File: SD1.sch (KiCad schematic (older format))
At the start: 44 parts, among them J103 JST ZH 1.5mm 1x5, J107 FPC PMS, Q101 BSS138, Q102 PDTC114EU,115, SW103 Multidirection_Switch, U102 ER-TFTM028-4, U104 CC2652P, U106 EKMC1691111, U107 MCP23017, U108 BME280, U109 SCD30

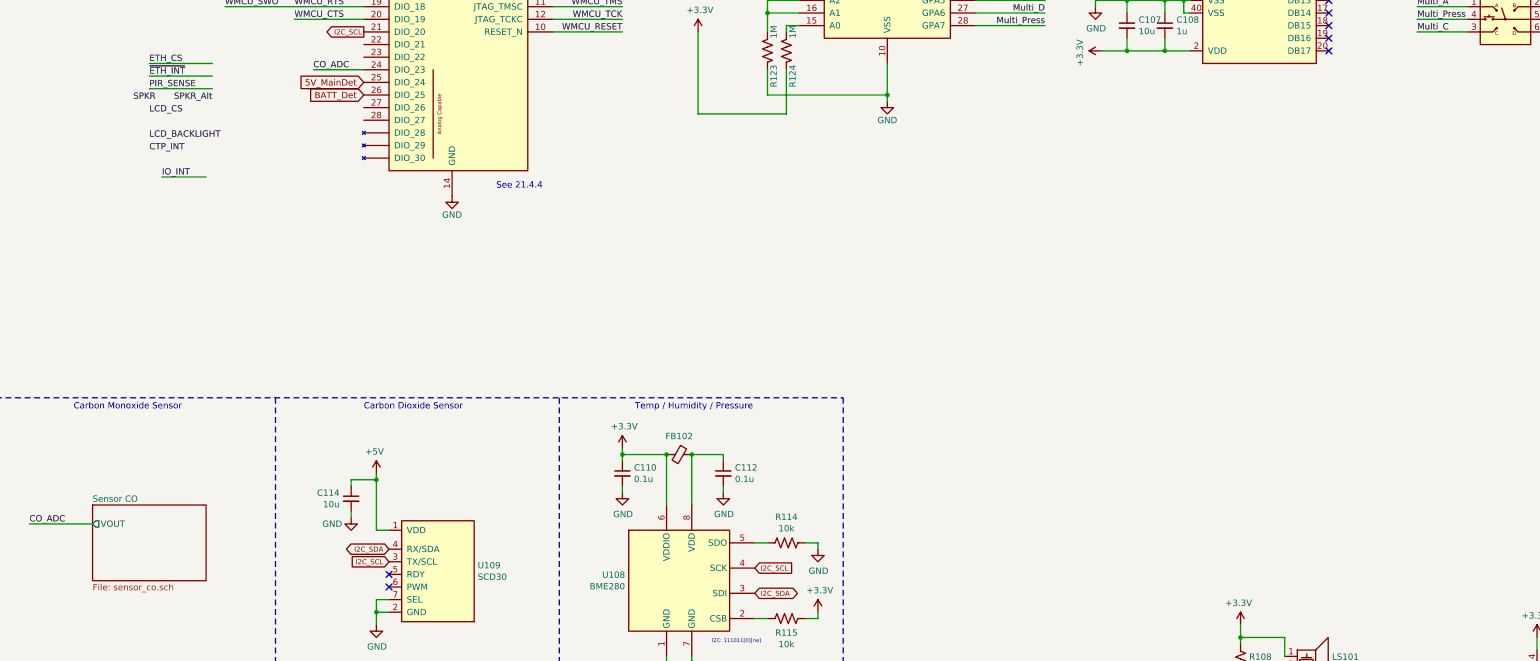
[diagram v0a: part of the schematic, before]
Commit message: Cleaned up, Annotated
Added Global 5V_Main net, solder jumper for battery charger, jumper for speaker and speaker_alt, added parts for battery charger
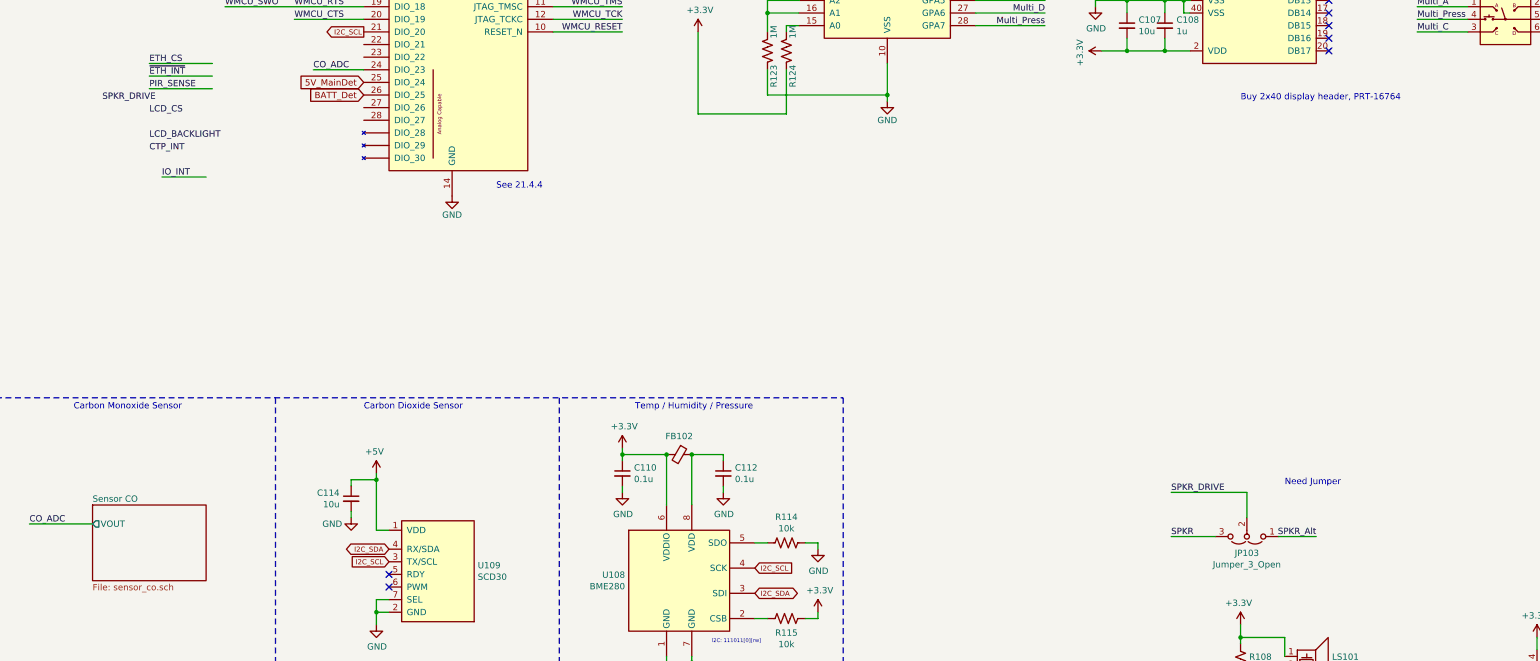
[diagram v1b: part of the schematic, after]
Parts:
- added JP103: Jumper_3_Open, Connector_PinHeader_2.54mm:PinHeader_1x03_P2.54mm_Vertical, symbol Jumper:Jumper_3_Open
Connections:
- net SPKR: now also JP103.3 (B)
- net SPKR_Alt: now also JP103.1 (A)
- new net SPKR_DRIVE: JP103.2 (C)
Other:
- note added: "Buy 2x40 display header, PRT-16764"
- note added: "Need Jumper"
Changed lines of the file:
@@
 Text Label 11200 3350 2    50   ~ 0
 Multi_Press
-Text Label 4600 3950 2    50   ~ 0
-SPKR_Alt
 Text Label 4150 3950 2    50   ~ 0
-SPKR
+SPKR_DRIVE
 Wire Wire Line
 	11150 2150 10650 2150
@@
 Wire Wire Line
 	15400 2500 15400 2550
+Text Notes 12750 3950 0    50   ~ 0
+Buy 2x40 display header, PRT-16764
+$Comp
+L Jumper:Jumper_3_Open JP103
+U 1 1 5FE23178
+P 12800 7400
+F 0 "JP103" H 12800 7531 50  0000 C CNN
+F 1 "Jumper_3_Open" H 12800 7622 50  0000 C CNN
+F 2 "Connector_PinHeader_2.54mm:PinHeader_1x03_P2.54mm_Vertical" H 12800 7400 50  0001 C CNN
+F 3 "~" H 12800 7400 50  0001 C CNN
+	1    12800 7400
+	-1   0    0    1
+$EndComp
+Wire Wire Line
+	12800 7250 12800 7050
+Wire Wire Line
+	12800 7050 12200 7050
+Wire Wire Line
+	13050 7400 13350 7400
+Wire Wire Line
+	12550 7400 12200 7400
+Text Label 12200 7400 0    50   ~ 0
+SPKR
+Text Label 13350 7400 2    50   ~ 0
+SPKR_Alt
+Text Label 12200 7050 0    50   ~ 0
+SPKR_DRIVE
+Text Notes 13100 7000 0    50   ~ 0
+Need Jumper
 $EndSCHEMATC

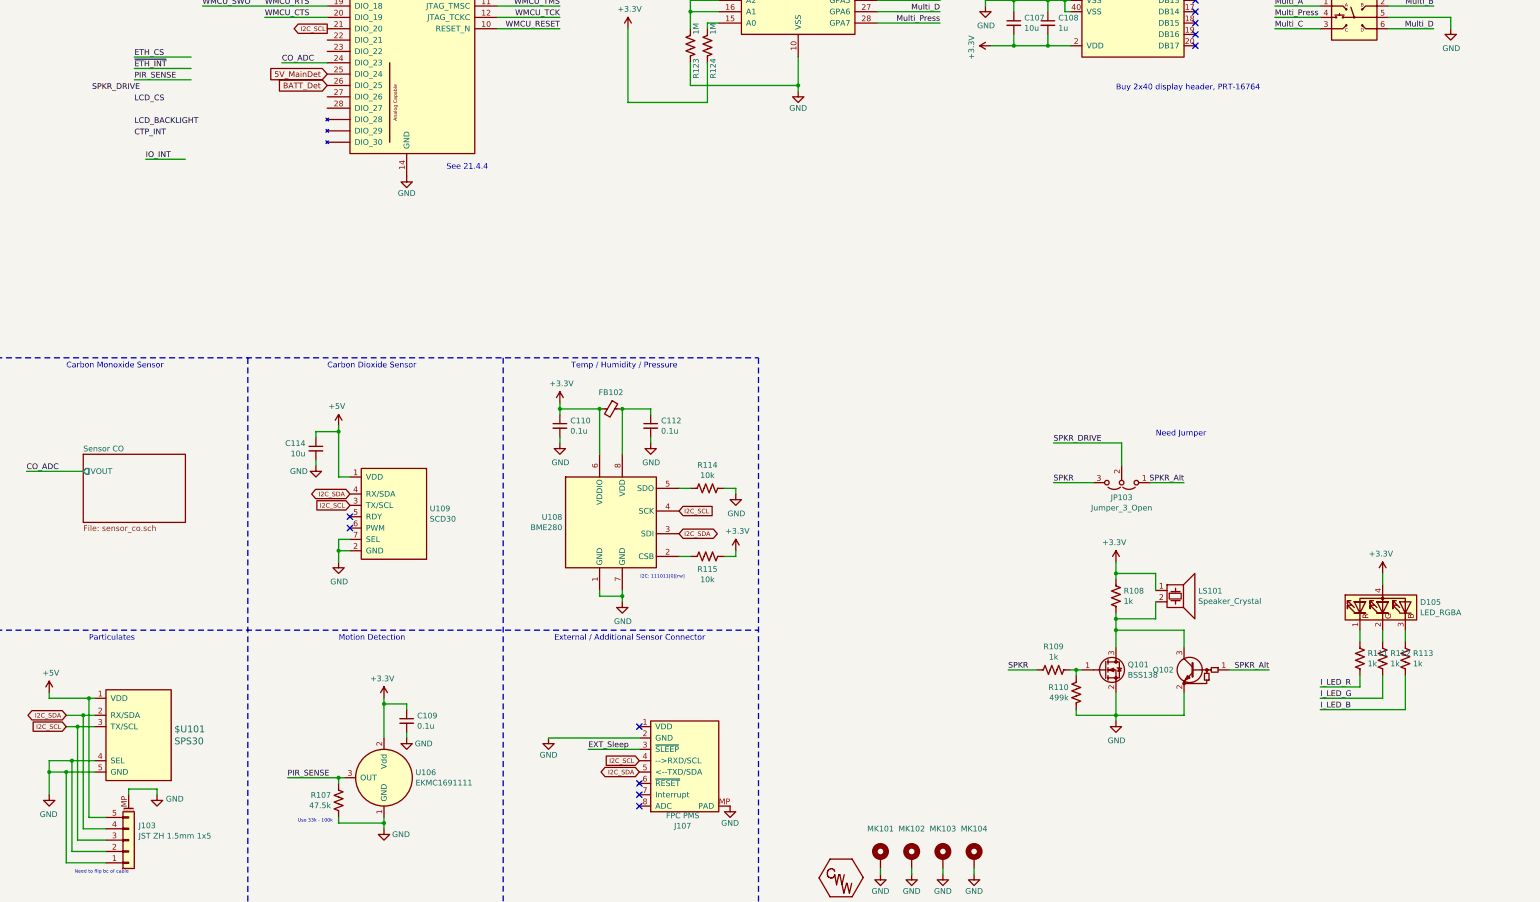
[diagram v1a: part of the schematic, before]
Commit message: Added RGBW connector
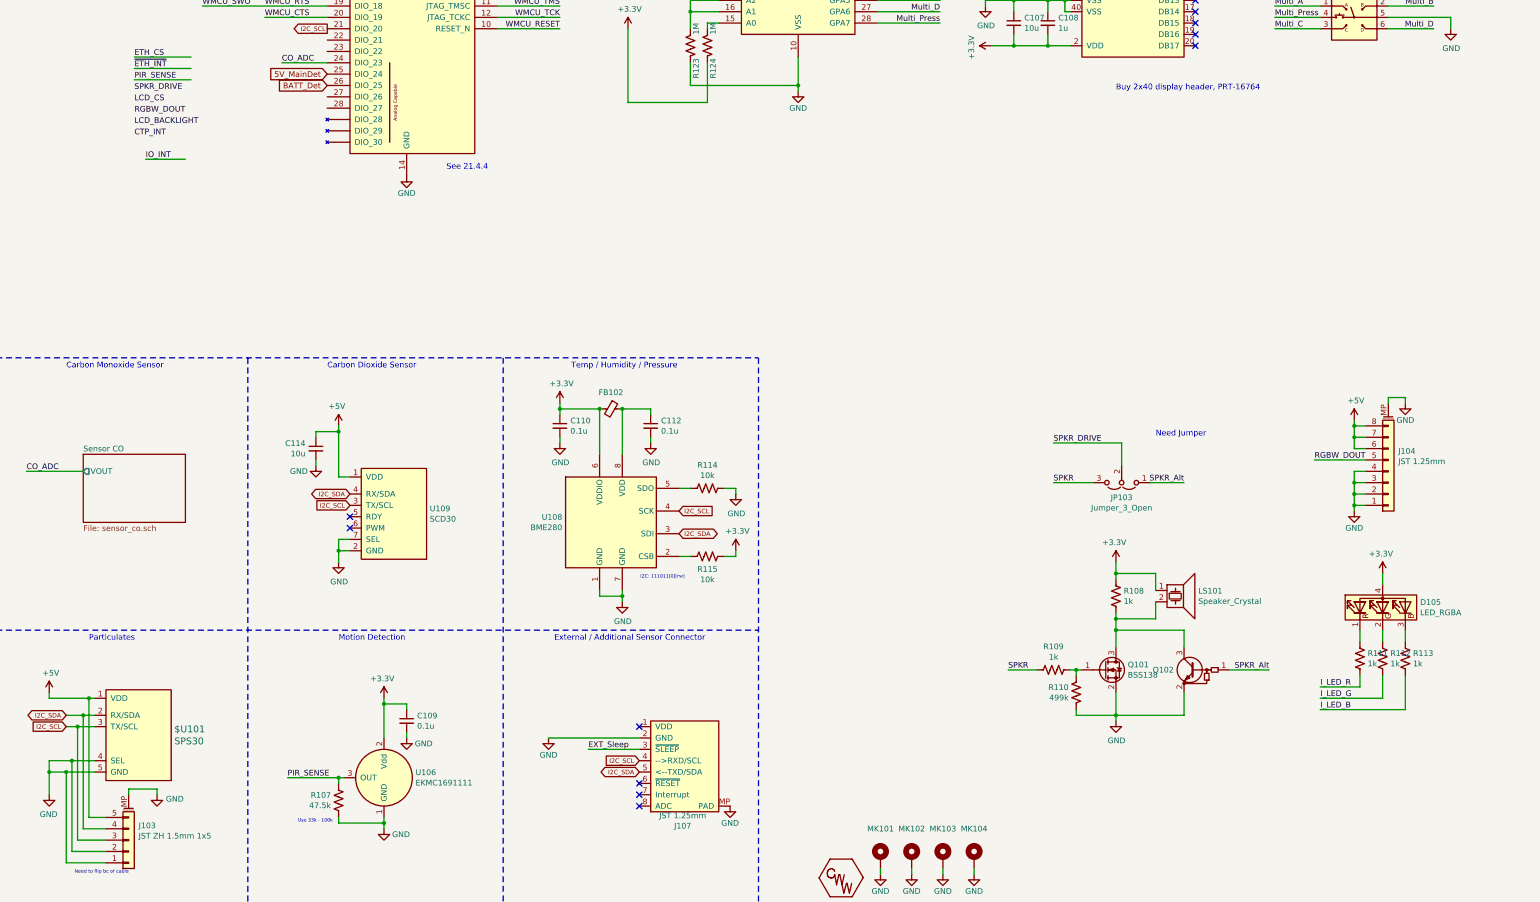
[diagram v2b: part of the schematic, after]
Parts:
- added J104: JST 1.25mm, Connector_Molex:Molex_PicoBlade_53398-0871_1x08-1MP_P1.25mm_Vertical, symbol Connector_Generic_MountingPin:Conn_01x08_MountingPin
- J107: value FPC PMS -> JST 1.25mm
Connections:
- net +5V: now also J104.6 (Pin_6), J104.7 (Pin_7), J104.8 (Pin_8)
- net GND: now also J104.1 (Pin_1), J104.2 (Pin_2), J104.3 (Pin_3), J104.4 (Pin_4), J104.MP (MountPin)
- new net RGBW_DOUT: J104.5 (Pin_5)
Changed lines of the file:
@@
 AR Path="/5FAEBA7D" Ref="J107"  Part="1"
 F 0 "J107" H 8768 9175 50  0000 C CNN
-F 1 "FPC PMS" H 8768 9266 50  0000 C CNN
+F 1 "JST 1.25mm" H 8768 9266 50  0000 C CNN
 F 2 "Connector_Molex:Molex_PicoBlade_53398-0871_1x08-1MP_P1.25mm_Vertical" H 8850 9800 50  0001 C CNN
 F 3 "" H 8850 9800 50  0001 C CNN
@@
 Text Label 11200 3350 2    50   ~ 0
 Multi_Press
-Text Label 4150 3950 2    50   ~ 0
+Text Label 4100 3950 0    50   ~ 0
 SPKR_DRIVE
 Wire Wire Line
@@
 Text Notes 13100 7000 0    50   ~ 0
 Need Jumper
+$Comp
+L Connector_Generic_MountingPin:Conn_01x08_MountingPin J104
+U 1 1 5FBD4208
+P 15150 7300
+F 0 "J104" H 15238 7122 50  0000 L CNN
+F 1 "JST 1.25mm" H 15238 7213 50  0000 L CNN
+F 2 "Connector_Molex:Molex_PicoBlade_53398-0871_1x08-1MP_P1.25mm_Vertical" H 15150 7300 50  0001 C CNN
+F 3 "~" H 15150 7300 50  0001 C CNN
+F 4 "WM7612CT-ND" H 15150 7300 50  0001 C CNN "Digikey"
+F 5 "0533980871" H 15150 7300 50  0001 C CNN "MPN"
+	1    15150 7300
+	1    0    0    1
+$EndComp
+$Comp
+L power:GND #PWR0206
+U 1 1 5FBD58B4
+P 15300 6700
+F 0 "#PWR0206" H 15300 6450 50  0001 C CNN
+F 1 "GND" H 15300 6550 50  0000 C CNN
+F 2 "" H 15300 6700 50  0001 C CNN
+F 3 "" H 15300 6700 50  0001 C CNN
+	1    15300 6700
+	-1   0    0    -1
+$EndComp
+$Comp
+L power:+5V #PWR?
+U 1 1 5FBD8B1F
+P 14850 6850
+AR Path="/5FAF778C/5FBD8B1F" Ref="#PWR?"  Part="1"
+AR Path="/5FBD8B1F" Ref="#PWR0207"  Part="1"
+F 0 "#PWR0207" H 14850 6700 50  0001 C CNN
+F 1 "+5V" H 14865 7023 50  0000 C CNN
+F 2 "" H 14850 6850 50  0001 C CNN
+F 3 "" H 14850 6850 50  0001 C CNN
+	1    14850 6850
+	1    0    0    -1
+$EndComp
+Wire Wire Line
+	14950 6900 14850 6900
+Wire Wire Line
+	14950 7000 14850 7000
+Wire Wire Line
+	14850 7000 14850 6900
+Connection ~ 14850 6900
+Wire Wire Line
+	14850 6900 14850 6850
+Wire Wire Line
+	14950 7100 14850 7100
+Wire Wire Line
+	14850 7100 14850 7000
+Connection ~ 14850 7000
+Wire Wire Line
+	15150 6700 15150 6650
+Wire Wire Line
+	15150 6650 15300 6650
+Wire Wire Line
+	15300 6650 15300 6700
+$Comp
+L power:GND #PWR0208
+U 1 1 5FC8FF7E
+P 14850 7650
+F 0 "#PWR0208" H 14850 7400 50  0001 C CNN
+F 1 "GND" H 14850 7500 50  0000 C CNN
+F 2 "" H 14850 7650 50  0001 C CNN
+F 3 "" H 14850 7650 50  0001 C CNN
+	1    14850 7650
+	-1   0    0    -1
+$EndComp
+Wire Wire Line
+	14950 7300 14850 7300
+Wire Wire Line
+	14850 7300 14850 7400
+Wire Wire Line
+	14950 7400 14850 7400
+Connection ~ 14850 7400
+Wire Wire Line
+	14850 7400 14850 7500
+Wire Wire Line
+	14950 7500 14850 7500
+Connection ~ 14850 7500
+Wire Wire Line
+	14850 7500 14850 7600
+Wire Wire Line
+	14950 7600 14850 7600
+Connection ~ 14850 7600
+Wire Wire Line
+	14850 7600 14850 7650
+Wire Wire Line
+	14950 7200 14500 7200
+Text Label 14500 7200 0    50   ~ 0
+RGBW_DOUT
+Text Label 4100 4150 0    50   ~ 0
+RGBW_DOUT
 $EndSCHEMATC

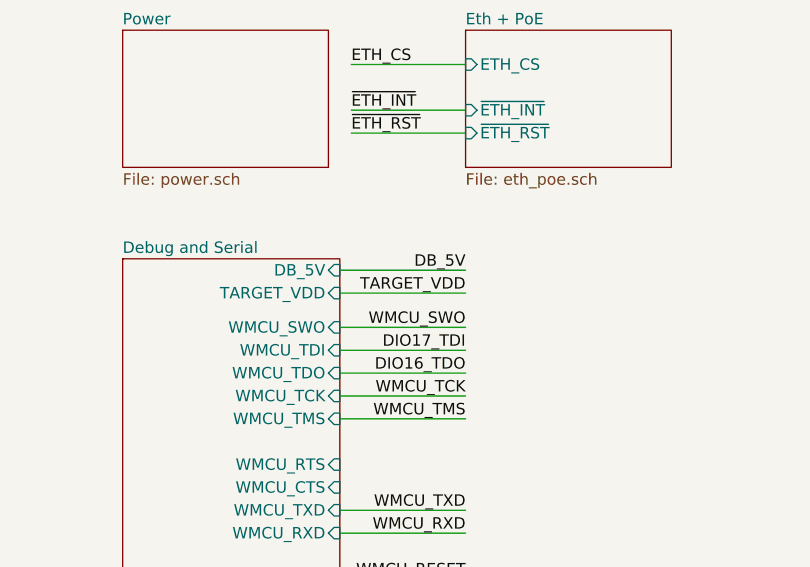
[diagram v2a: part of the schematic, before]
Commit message: Bugfix: critical net name error for target VDD and debugging connectors
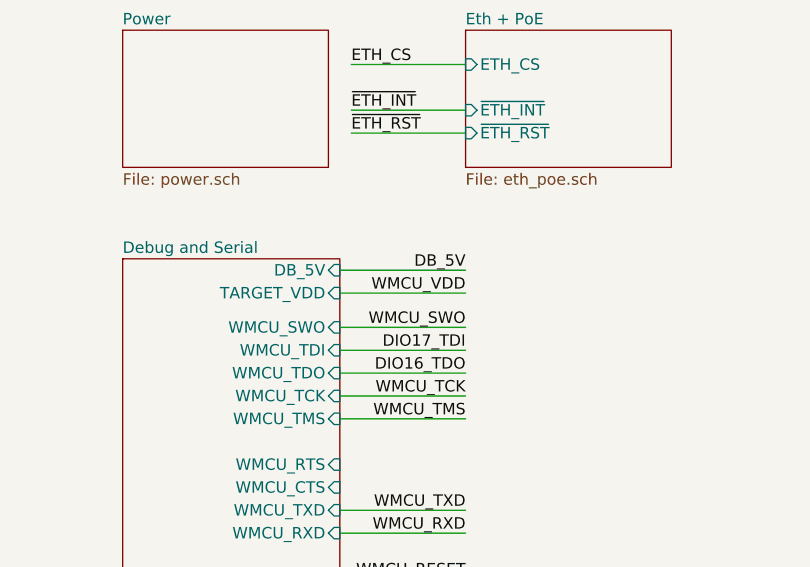
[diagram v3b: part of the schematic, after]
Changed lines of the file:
@@
 WMCU_SWO
 Text Label 2200 1850 2    50   ~ 0
-TARGET_VDD
+WMCU_VDD
 Wire Wire Line
 	2200 1850 1650 1850

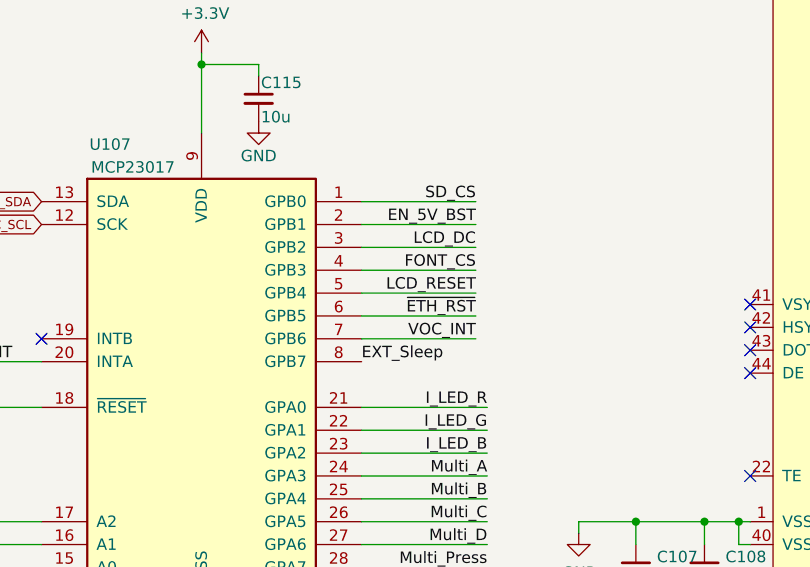
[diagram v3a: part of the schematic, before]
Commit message: Bugfix: net name error for LCD reset
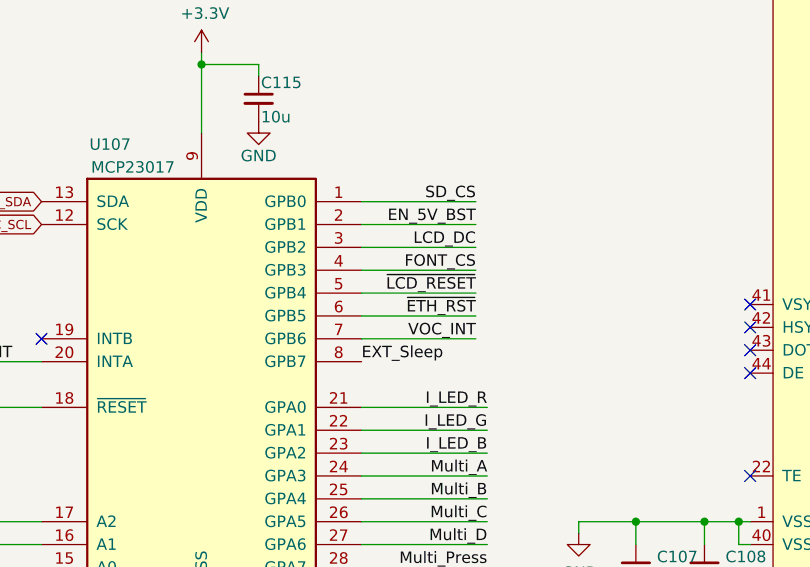
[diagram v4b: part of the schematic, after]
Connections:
- net LCD_RESET is gone; now on net ~LCD_RESET: U107.5 (GPB4)
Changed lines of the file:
@@
 ~LCD_RESET
 Text Label 11150 2150 2    50   ~ 0
-LCD_RESET
+~LCD_RESET
 $Comp
 L power:+3.3V #PWR?
